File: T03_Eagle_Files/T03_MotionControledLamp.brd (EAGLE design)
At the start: 63.5 x 43.2 mm, 30 parts, among them U1 ATMEGA328P-MU, U4 TPS61161ADRVT, X2 16MHz

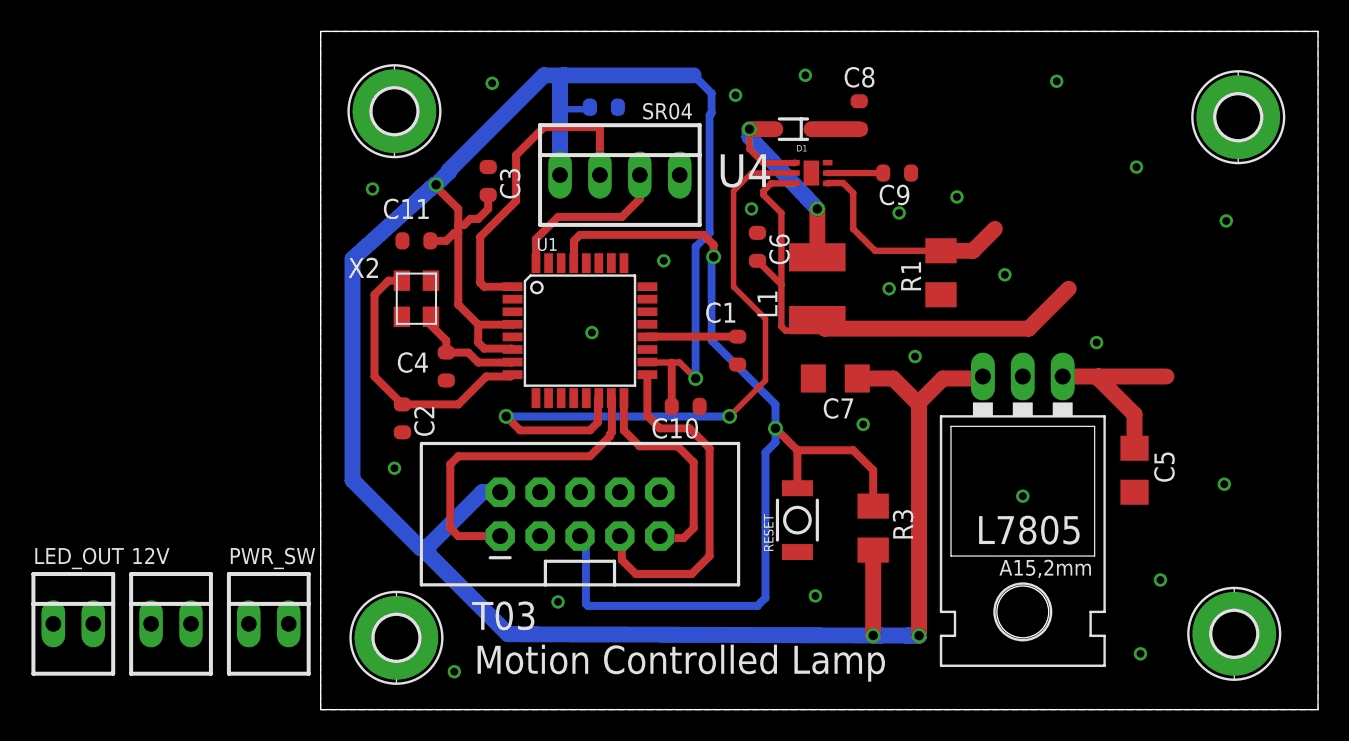
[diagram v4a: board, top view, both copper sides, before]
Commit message: Updated board layout for molex connects
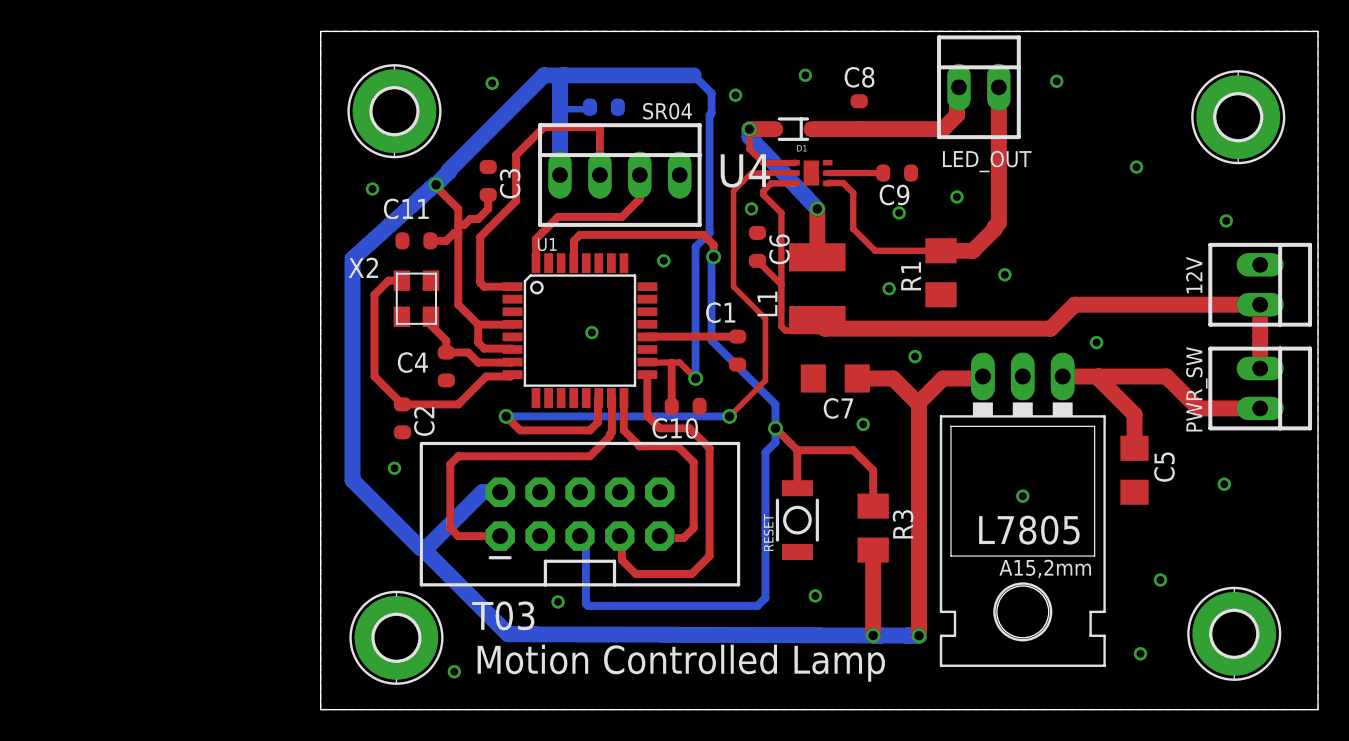
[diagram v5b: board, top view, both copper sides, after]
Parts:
- moved 12V 72.6 mm to (59.8, 27.1), turned to 270 degrees
- moved LED_OUT 67.0 mm to (41.9, 39.6)
- moved PWR_SW 64.9 mm to (59.8, 20.4), turned to 270 degrees
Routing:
- net +V_BAT: track 33.7 -> 49.5 mm
- net FB: track 14.4 -> 23.5 mm
- net LED_V+: track 3.04 -> 11.5 mm
- net N$4: track 12.1 -> 18.9 mm
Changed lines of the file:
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@@
 </element>
 <element name="C12" library="Smartprj" package="C0603-ROUND" value="0.1uF" x="18.034" y="38.354" rot="MR0"/>
-<element name="PWR_SW" library="con-molex" package="22-23-2021" value="22-23-2021" x="-3.302" y="5.461">
-<attribute name="OC_FARNELL" value="1462926" x="-3.302" y="5.461" size="1.778" layer="27" display="off"/>
-<attribute name="MPN" value="22-23-2021" x="-3.302" y="5.461" size="1.778" layer="27" display="off"/>
-<attribute name="MF" value="MOLEX" x="-3.302" y="5.461" size="1.778" layer="27" display="off"/>
-<attribute name="OC_NEWARK" value="25C3832" x="-3.302" y="5.461" size="1.778" layer="27" display="off"/>
+<element name="PWR_SW" library="con-molex" package="22-23-2021" value="22-23-2021" x="59.817" y="20.447" smashed="yes" rot="R270">
+<attribute name="OC_FARNELL" value="1462926" x="59.817" y="20.447" size="1.778" layer="27" rot="R270" display="off"/>
+<attribute name="MPN" value="22-23-2021" x="59.817" y="20.447" size="1.778" layer="27" rot="R270" display="off"/>
+<attribute name="MF" value="MOLEX" x="59.817" y="20.447" size="1.778" layer="27" rot="R270" display="off"/>
+<attribute name="OC_NEWARK" value="25C3832" x="59.817" y="20.447" size="1.778" layer="27" rot="R270" display="off"/>
+<attribute name="NAME" x="55.118" y="23.114" size="1.016" layer="25" ratio="10" rot="R270"/>
+<attribute name="VALUE" x="54.737" y="22.987" size="1.016" layer="27" ratio="10" rot="R270"/>
 </element>
-<element name="12V" library="con-molex" package="22-23-2021" value="22-23-2021" x="-9.525" y="5.461">
-<attribute name="OC_FARNELL" value="1462926" x="-9.525" y="5.461" size="1.778" layer="27" display="off"/>
-<attribute name="MPN" value="22-23-2021" x="-9.525" y="5.461" size="1.778" layer="27" display="off"/>
-<attribute name="MF" value="MOLEX" x="-9.525" y="5.461" size="1.778" layer="27" display="off"/>
-<attribute name="OC_NEWARK" value="25C3832" x="-9.525" y="5.461" size="1.778" layer="27" display="off"/>
+<element name="12V" library="con-molex" package="22-23-2021" value="22-23-2021" x="59.817" y="27.051" smashed="yes" rot="R270">
+<attribute name="OC_FARNELL" value="1462926" x="59.817" y="27.051" size="1.778" layer="27" rot="R270" display="off"/>
+<attribute name="MPN" value="22-23-2021" x="59.817" y="27.051" size="1.778" layer="27" rot="R270" display="off"/>
+<attribute name="MF" value="MOLEX" x="59.817" y="27.051" size="1.778" layer="27" rot="R270" display="off"/>
+<attribute name="OC_NEWARK" value="25C3832" x="59.817" y="27.051" size="1.778" layer="27" rot="R270" display="off"/>
+<attribute name="NAME" x="55.118" y="28.829" size="1.016" layer="25" ratio="10" rot="R270"/>
+<attribute name="VALUE" x="54.737" y="29.591" size="1.016" layer="27" ratio="10" rot="R270"/>
 </element>
-<element name="LED_OUT" library="con-molex" package="22-23-2021" value="22-23-2021" x="-15.748" y="5.461">
-<attribute name="OC_FARNELL" value="1462926" x="-15.748" y="5.461" size="1.778" layer="27" display="off"/>
-<attribute name="MPN" value="22-23-2021" x="-15.748" y="5.461" size="1.778" layer="27" display="off"/>
-<attribute name="MF" value="MOLEX" x="-15.748" y="5.461" size="1.778" layer="27" display="off"/>
-<attribute name="OC_NEWARK" value="25C3832" x="-15.748" y="5.461" size="1.778" layer="27" display="off"/>
+<element name="LED_OUT" library="con-molex" package="22-23-2021" value="22-23-2021" x="41.91" y="39.624" smashed="yes">
+<attribute name="OC_FARNELL" value="1462926" x="41.91" y="39.624" size="1.778" layer="27" display="off"/>
+<attribute name="MPN" value="22-23-2021" x="41.91" y="39.624" size="1.778" layer="27" display="off"/>
+<attribute name="MF" value="MOLEX" x="41.91" y="39.624" size="1.778" layer="27" display="off"/>
+<attribute name="OC_NEWARK" value="25C3832" x="41.91" y="39.624" size="1.778" layer="27" display="off"/>
+<attribute name="NAME" x="39.497" y="34.544" size="1.016" layer="25" ratio="10"/>
+<attribute name="VALUE" x="39.37" y="34.544" size="1.016" layer="27" ratio="10"/>
 </element>
 </elements>
@@
 <via x="44.704" y="13.589" extent="1-16" drill="0.5"/>
 <contactref element="12V" pad="1"/>
-<wire x1="4.699" y1="15.367" x2="-10.795" y2="5.461" width="0" layer="19" extent="1-1"/>
 </signal>
 <signal name="AREF">
@@
 <wire x1="49.53" y1="21.082" x2="49.53" y2="21.209" width="1.016" layer="1"/>
 <contactref element="PWR_SW" pad="2"/>
-<wire x1="-2.032" y1="5.461" x2="47.244" y2="21.209" width="0" layer="19" extent="1-1"/>
+<wire x1="59.817" y1="19.177" x2="55.88" y2="19.177" width="1.016" layer="1"/>
+<wire x1="55.88" y1="19.177" x2="53.848" y2="21.209" width="1.016" layer="1"/>
 </signal>
 <signal name="RST">
@@
 <wire x1="31.249" y1="36.957" x2="34.29" y2="36.957" width="1.016" layer="1"/>
 <contactref element="LED_OUT" pad="1"/>
-<wire x1="-17.018" y1="5.461" x2="31.249" y2="36.957" width="0" layer="19" extent="1-1"/>
+<wire x1="34.29" y1="36.957" x2="39.624" y2="36.957" width="1.016" layer="1"/>
+<wire x1="39.624" y1="36.957" x2="40.513" y2="37.846" width="1.016" layer="1"/>
+<wire x1="40.513" y1="37.846" x2="40.513" y2="39.497" width="1.016" layer="1"/>
+<wire x1="40.513" y1="39.497" x2="40.64" y2="39.624" width="1.016" layer="1"/>
 </signal>
 <signal name="FB">
@@
 <wire x1="41.529" y1="29.21" x2="42.926" y2="30.607" width="1.016" layer="1"/>
 <contactref element="LED_OUT" pad="2"/>
-<wire x1="-14.478" y1="5.461" x2="32.2834" y2="33.5026" width="0" layer="19" extent="1-1"/>
+<wire x1="42.926" y1="30.607" x2="42.926" y2="30.734" width="1.016" layer="1"/>
+<wire x1="42.926" y1="30.734" x2="43.18" y2="30.988" width="1.016" layer="1"/>
+<wire x1="43.18" y1="30.988" x2="43.18" y2="39.624" width="1.016" layer="1"/>
 </signal>
 <signal name="COMP">
@@
 <contactref element="L1" pad="1"/>
 <wire x1="31.623" y1="24.797" x2="32.099" y2="24.257" width="1.016" layer="1"/>
-<wire x1="32.099" y1="24.257" x2="45.085" y2="24.257" width="1.016" layer="1"/>
-<wire x1="45.085" y1="24.257" x2="47.625" y2="26.797" width="1.016" layer="1"/>
+<wire x1="32.099" y1="24.257" x2="46.482" y2="24.257" width="1.016" layer="1"/>
 <wire x1="32.099" y1="24.257" x2="31.972" y2="24.13" width="0.4064" layer="1"/>
 <wire x1="31.972" y1="24.13" x2="29.591" y2="24.13" width="0.4064" layer="1"/>
@@
 <contactref element="12V" pad="2"/>
 <contactref element="PWR_SW" pad="1"/>
-<wire x1="-4.572" y1="5.461" x2="29.337" y2="24.384" width="0" layer="19" extent="1-1"/>
-<wire x1="-8.255" y1="5.461" x2="-4.572" y2="5.461" width="0" layer="19" extent="1-1"/>
+<wire x1="46.482" y1="24.257" x2="48.006" y2="25.781" width="1.016" layer="1"/>
+<wire x1="48.006" y1="25.781" x2="59.817" y2="25.781" width="1.016" layer="1"/>
+<wire x1="59.817" y1="25.781" x2="59.817" y2="21.717" width="1.016" layer="1"/>
 </signal>
 <signal name="TRIG">
